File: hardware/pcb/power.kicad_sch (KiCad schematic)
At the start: 9 parts, among them J1 USB_C_Receptacle_USB2.0_14P, U1 AMS1117-3.3, U2 USBLC6-2SC6

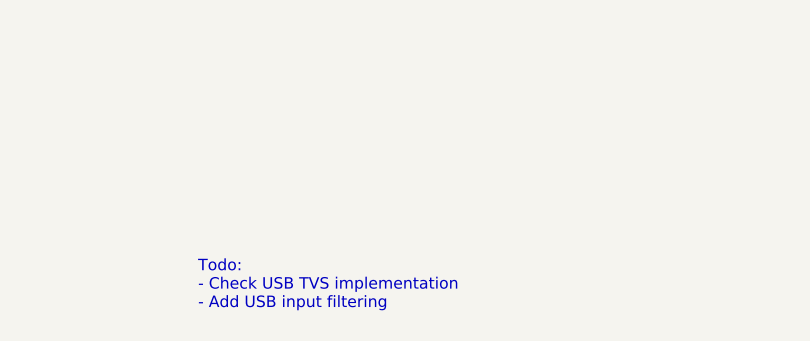
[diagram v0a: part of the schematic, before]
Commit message: draft: Added ESP32 and connector
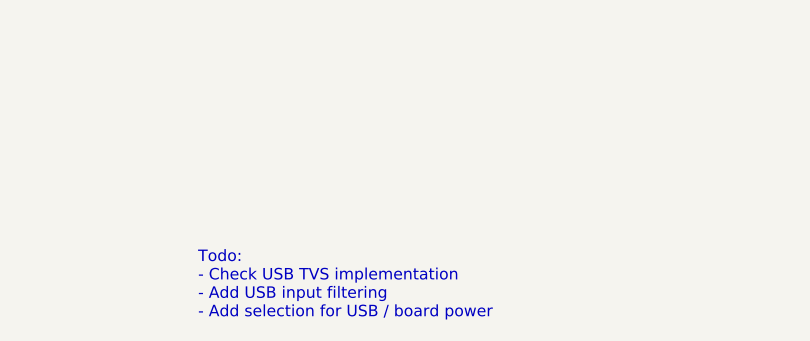
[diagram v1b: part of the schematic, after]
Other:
- note added: "Todo: - Check USB TVS implementation - Add USB input filtering - Add selection for USB / board power"
- note removed: "Todo: - Check USB TVS implementation - Add USB input filtering"
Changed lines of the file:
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@@
 		)
 	)
-	(text "Todo:\n- Check USB TVS implementation\n- Add USB input filtering"
+	(text "Todo:\n- Check USB TVS implementation\n- Add USB input filtering\n- Add selection for USB / board power"
 		(exclude_from_sim no)
 		(at 178.562 170.434 0)
